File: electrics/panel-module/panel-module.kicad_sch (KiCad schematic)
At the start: 17 parts, among them J1 East, J2 West, J4 Display, SW1 Setup, SW2 Reset

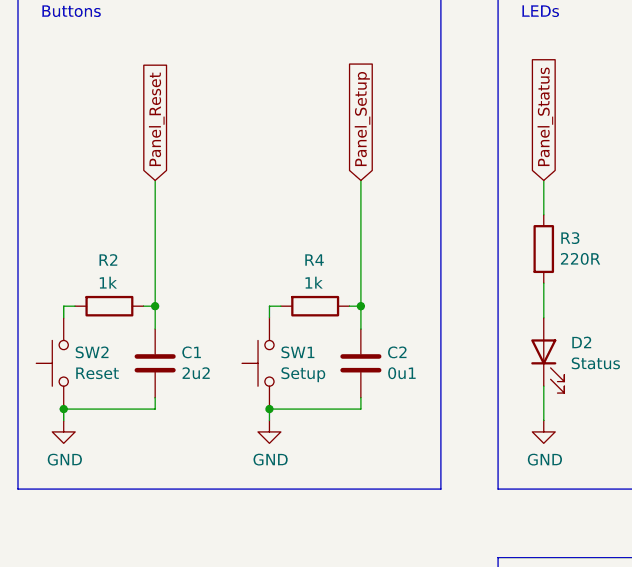
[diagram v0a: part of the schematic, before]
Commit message: Added product numbers for cost calculation
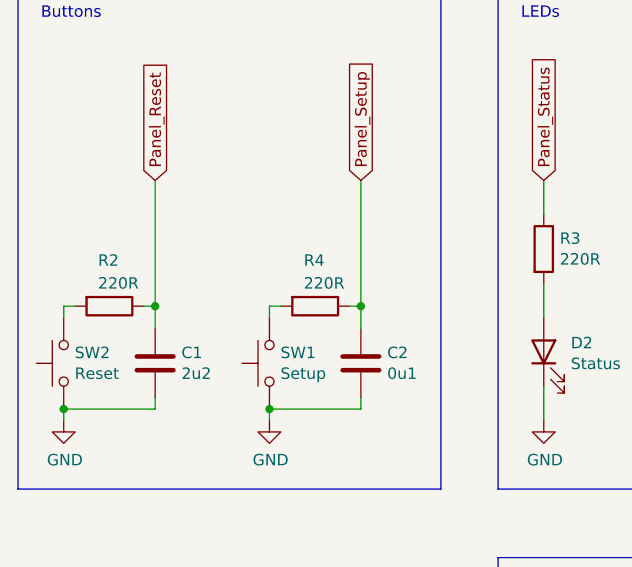
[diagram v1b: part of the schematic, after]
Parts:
- C1: Price 0.07 -> (none); Product https://www.mouser.de/ProductDetail/Taiyo-Yuden/TMK316BJ225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 -> (none); manf# (none) -> TMK316BJ225KD-T; mouser# (none) -> 963-TMK316BJ225KD-T; part-num (none) -> TMK316BJ225KD-T
- D1, D2: Price 0.06 -> (none); Product https://www.mouser.de/ProductDetail/Lite-On/LTST-C150GKT -> (none); manf# (none) -> SML-LXL1206GC-TR; mouser# (none) -> 696-SML-L1206GCTR; part-num LTST-C150GKT -> SML-LXL1206GC-TR
- G1, H1, H2, J1, J2, J4: Price 0 -> (none); Product N/A -> (none)
- R1, R3: Price 0.08 -> (none); Product https://www.mouser.de/ProductDetail/Vishay-Draloric/RCG1206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 -> (none); mouser# (none) -> 71-RCG1206220RJNEA
- R2, R4: value 1k -> 220R; Price 0.08 -> (none); Product https://www.mouser.de/ProductDetail/Vishay-Draloric/RCG1206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 -> (none); manf# (none) -> RCG1206220RJNEA; mouser# (none) -> 71-RCG1206220RJNEA
- SW1, SW2: Price 0.47 -> (none); Product https://www.mouser.de/ProductDetail/CK/PTS645SK43SMTR92LFS -> (none); manf# (none) -> PTS645SK43SMTR92LFS; mouser# (none) -> 611-PTS645SK43SMTR92; part-num (none) -> PTS645SK43SMTR92LFS

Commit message: M bus module (#12)
* Fix wrong resistor manufacturer number in panel module

* Added missing labels for bus connectors in "Mieterstrom" module

* Added missing 3D model for BC66NB

* Finalized PoC for M-Bus module

* Updated documentation
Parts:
- SW1, SW2: mouser# 611-PTS645SK43SMTR92 -> 611-RS014R05B1SMA10R
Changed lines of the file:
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@@
       (effects (font (size 1.27 1.27)) hide)
     )
-    (property "mouser#" "611-PTS645SK43SMTR92" (id 5) (at 66.04 76.2 0)
+    (property "mouser#" "611-RS014R05B1SMA10R" (id 5) (at 66.04 76.2 0)
       (effects (font (size 1.27 1.27)) hide)
     )
@@
       (effects (font (size 1.27 1.27)) hide)
     )
-    (property "mouser#" "611-PTS645SK43SMTR92" (id 7) (at 88.9 76.2 0)
-      (effects (font (size 1.27 1.27)) hide)
-    )
+    (property "mouser#" "611-RS014R05B1SMA10R" (id 7) (at 88.9 76.2 0)
+      (effects (font (size 1.27 1.27)) hide)
+    )

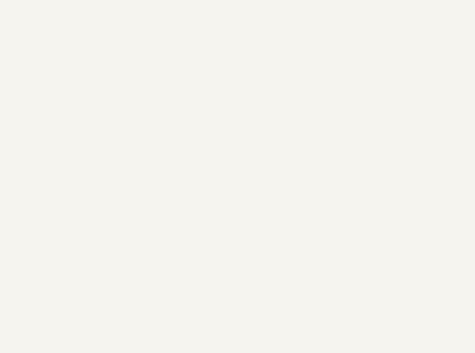
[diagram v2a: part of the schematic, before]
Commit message: Fix all ERC and DRC warnings during build
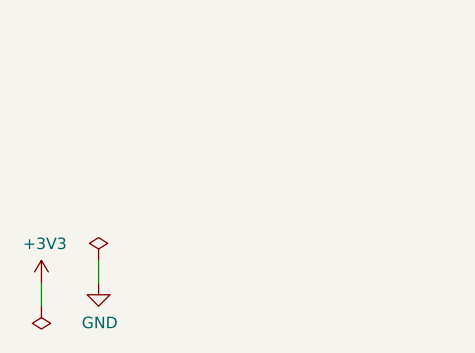
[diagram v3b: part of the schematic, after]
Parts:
- D1, D2: Manf# LTST-C150GKT -> (none)
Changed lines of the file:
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@@
+    (stroke (width 0) (type default) (color 0 0 0 0))
+  )
+  (wire (pts (xy 25.4 181.61) (xy 25.4 184.15))
     (stroke (width 0) (type default) (color 0 0 0 0))
   )
@@
   )
   (wire (pts (xy 200.66 55.88) (xy 207.01 55.88))
+    (stroke (width 0) (type default) (color 0 0 0 0))
+  )
+  (wire (pts (xy 31.75 179.07) (xy 31.75 181.61))
     (stroke (width 0) (type default) (color 0 0 0 0))
   )
@@
     )
     (property "Datasheet" "https://www.mouser.de/datasheet/2/244/LUMX_S_A0003593352_1-2551948.pdf" (id 3) (at 119.38 74.93 0)
-      (effects (font (size 1.27 1.27)) hide)
-    )
-    (property "Manf#" "LTST-C150GKT" (id 6) (at 119.38 74.93 90)
       (effects (font (size 1.27 1.27)) hide)
     )
@@
       (effects (font (size 1.27 1.27)) hide)
     )
-    (property "Manf#" "LTST-C150GKT" (id 6) (at 135.89 74.93 90)
-      (effects (font (size 1.27 1.27)) hide)
-    )
     (property "part-num" "SML-LXL1206GC-TR" (id 7) (at 135.89 74.93 0)
       (effects (font (size 1.27 1.27)) hide)
@@
     (pin "1")
   )
+  (symbol (lib_id "power:GND") (at 31.75 181.61 0) (unit 1)
+    (in_bom yes) (on_board yes)
+    (property "Reference" "#PWR?" (id 0) (at 31.75 187.96 0)
+      (effects (font (size 1.27 1.27)) hide)
+    )
+    (property "Value" "GND" (id 1) (at 31.877 186.0042 0))
+    (property "Footprint" "" (id 2) (at 31.75 181.61 0)
+      (effects (font (size 1.27 1.27)) hide)
+    )
+    (property "Datasheet" "" (id 3) (at 31.75 181.61 0)
+      (effects (font (size 1.27 1.27)) hide)
+    )
+    (pin "1")
+  )
+  (symbol (lib_id "power:+3V3") (at 25.4 181.61 0) (unit 1)
+    (in_bom yes) (on_board yes)
+    (property "Reference" "#PWR?" (id 0) (at 25.4 185.42 0)
+      (effects (font (size 1.27 1.27)) hide)
+    )
+    (property "Value" "+3V3" (id 1) (at 25.781 177.2158 0))
+    (property "Footprint" "" (id 2) (at 25.4 181.61 0)
+      (effects (font (size 1.27 1.27)) hide)
+    )
+    (property "Datasheet" "" (id 3) (at 25.4 181.61 0)
+      (effects (font (size 1.27 1.27)) hide)
+    )
+    (pin "1")
+  )
+  (symbol (lib_id "power:PWR_FLAG") (at 31.75 179.07 0) (unit 1)
+    (in_bom yes) (on_board yes) (fields_autoplaced)
+    (property "Reference" "#FLG?" (id 0) (at 31.75 177.165 0)
+      (effects (font (size 1.27 1.27)) hide)
+    )
+    (property "Value" "PWR_FLAG" (id 1) (at 31.75 173.99 0)
+      (effects (font (size 1.27 1.27)) hide)
+    )
+    (property "Footprint" "" (id 2) (at 31.75 179.07 0)
+      (effects (font (size 1.27 1.27)) hide)
+    )
+    (property "Datasheet" "~" (id 3) (at 31.75 179.07 0)
+      (effects (font (size 1.27 1.27)) hide)
+    )
+    (pin "1")
+  )
+  (symbol (lib_id "power:PWR_FLAG") (at 25.4 184.15 180) (unit 1)
+    (in_bom yes) (on_board yes) (fields_autoplaced)
+    (property "Reference" "#FLG?" (id 0) (at 25.4 186.055 0)
+      (effects (font (size 1.27 1.27)) hide)
+    )
+    (property "Value" "PWR_FLAG" (id 1) (at 25.4 189.23 0)
+      (effects (font (size 1.27 1.27)) hide)
+    )
+    (property "Footprint" "" (id 2) (at 25.4 184.15 0)
+      (effects (font (size 1.27 1.27)) hide)
+    )
+    (property "Datasheet" "~" (id 3) (at 25.4 184.15 0)
+      (effects (font (size 1.27 1.27)) hide)
+    )
+    (pin "1")
+  )
   (sheet_instances
     (path "/" (page "1"))
   )
   (symbol_instances
+    (path "/b33109e2-825f-486d-8082-bb53c640cf03"
+      (reference "#FLG?") (unit 1) (value "PWR_FLAG") (footprint "")
+    )
+    (path "/e1c72263-fb7a-4cf6-a780-f5500b0d2137"
+      (reference "#FLG?") (unit 1) (value "PWR_FLAG") (footprint "")
+    )
     (path "/00000000-0000-0000-0000-000061d7aff4"
       (reference "#PWR0101") (unit 1) (value "+3V3") (footprint "")
@@
       (reference "#PWR0113") (unit 1) (value "GND") (footprint "")
     )
+    (path "/1f0b9008-dbd8-4274-9a87-24fba18ad79f"
+      (reference "#PWR?") (unit 1) (value "GND") (footprint "")
+    )
+    (path "/6710d8e4-d663-46cc-bf3d-426926181414"
+      (reference "#PWR?") (unit 1) (value "+3V3") (footprint "")
+    )
     (path "/00000000-0000-0000-0000-0000622f8d63"
